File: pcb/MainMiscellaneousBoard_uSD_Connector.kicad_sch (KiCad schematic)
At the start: 10 parts, among them J1 0472192001

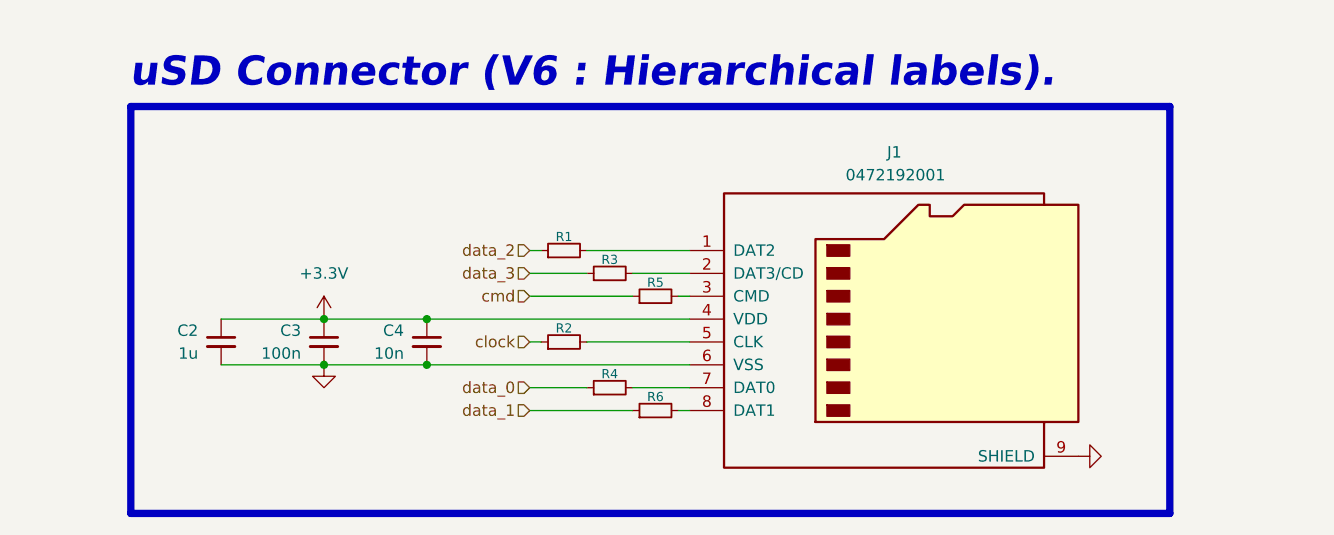
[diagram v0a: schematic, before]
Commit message: Updated `StackConnector` to use reference prefix of "J".
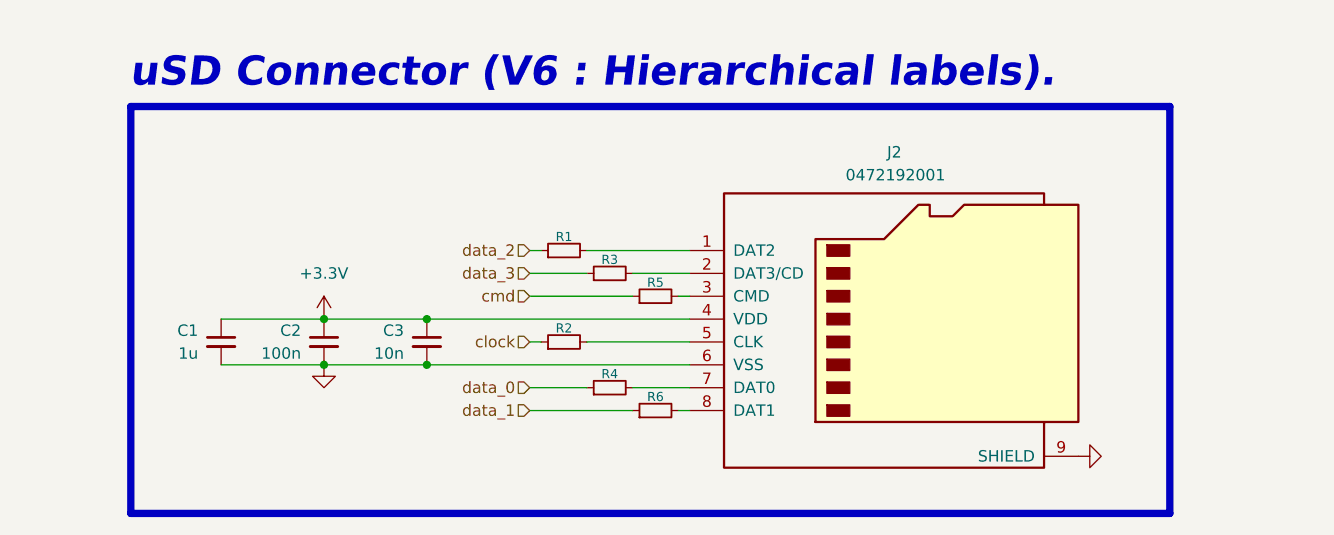
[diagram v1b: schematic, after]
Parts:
- renumbered C2 to C1, C3 to C2, C4 to C3, J1 to J2
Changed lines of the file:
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@@
 		(on_board yes)
 		(dnp no)
-		(property "Reference" "C2"
+		(property "Reference" "C1"
 			(at 52.07 78.7462 0)
 			(effects
@@
 			(project "MainMiscellaneousBoard"
 				(path "/98fc9565-7d66-4cd3-b0d6-fc60566bea9b/4f2e1eb9-ac73-426b-a6fe-8e3837c7983e"
-					(reference "C5")
-					(unit 1)
-				)
-				(path "/98fc9565-7d66-4cd3-b0d6-fc60566bea9b/5d94b41c-643f-433f-ba9e-5a80a87c9806"
-					(reference "C2")
+					(reference "C4")
+					(unit 1)
+				)
+				(path "/98fc9565-7d66-4cd3-b0d6-fc60566bea9b/5d94b41c-643f-433f-ba9e-5a80a87c9806"
+					(reference "C1")
 					(unit 1)
 				)
@@
 		(on_board yes)
 		(dnp no)
-		(property "Reference" "C3"
+		(property "Reference" "C2"
 			(at 63.5 78.7462 0)
 			(effects
@@
 			(project "MainMiscellaneousBoard"
 				(path "/98fc9565-7d66-4cd3-b0d6-fc60566bea9b/4f2e1eb9-ac73-426b-a6fe-8e3837c7983e"
-					(reference "C6")
-					(unit 1)
-				)
-				(path "/98fc9565-7d66-4cd3-b0d6-fc60566bea9b/5d94b41c-643f-433f-ba9e-5a80a87c9806"
-					(reference "C3")
+					(reference "C5")
+					(unit 1)
+				)
+				(path "/98fc9565-7d66-4cd3-b0d6-fc60566bea9b/5d94b41c-643f-433f-ba9e-5a80a87c9806"
+					(reference "C2")
 					(unit 1)
 				)
@@
 		(on_board yes)
 		(dnp no)
-		(property "Reference" "J1"
+		(property "Reference" "J2"
 			(at 129.413 58.928 0)
 			(effects
@@
 			(project "MainMiscellaneousBoard"
 				(path "/98fc9565-7d66-4cd3-b0d6-fc60566bea9b/4f2e1eb9-ac73-426b-a6fe-8e3837c7983e"
+					(reference "J3")
+					(unit 1)
+				)
+				(path "/98fc9565-7d66-4cd3-b0d6-fc60566bea9b/5d94b41c-643f-433f-ba9e-5a80a87c9806"
 					(reference "J2")
-					(unit 1)
-				)
-				(path "/98fc9565-7d66-4cd3-b0d6-fc60566bea9b/5d94b41c-643f-433f-ba9e-5a80a87c9806"
-					(reference "J1")
 					(unit 1)
 				)
@@
 		(on_board yes)
 		(dnp no)
-		(property "Reference" "C4"
+		(property "Reference" "C3"
 			(at 74.93 78.7462 0)
 			(effects
@@
 			(project "MainMiscellaneousBoard"
 				(path "/98fc9565-7d66-4cd3-b0d6-fc60566bea9b/4f2e1eb9-ac73-426b-a6fe-8e3837c7983e"
-					(reference "C7")
-					(unit 1)
-				)
-				(path "/98fc9565-7d66-4cd3-b0d6-fc60566bea9b/5d94b41c-643f-433f-ba9e-5a80a87c9806"
-					(reference "C4")
-					(unit 1)
-				)
+					(reference "C6")
+					(unit 1)
+				)
+				(path "/98fc9565-7d66-4cd3-b0d6-fc60566bea9b/5d94b41c-643f-433f-ba9e-5a80a87c9806"
+					(reference "C3")
+					(unit 1)
+				)

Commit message: Made symbol for ItsyBitsy ESP32.
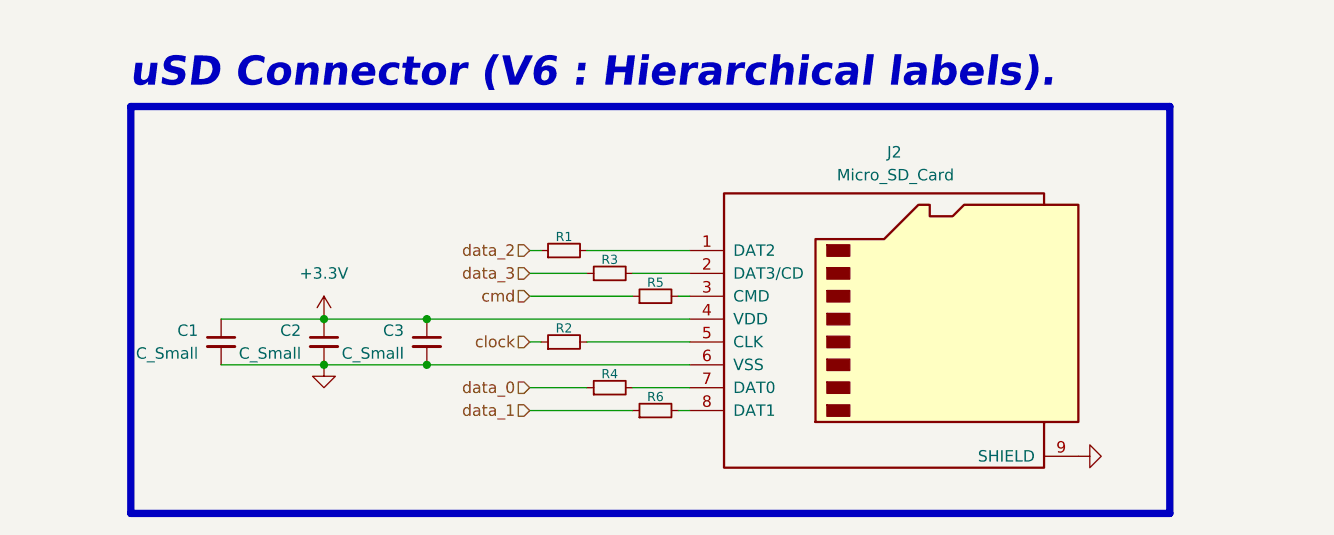
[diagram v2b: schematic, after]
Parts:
- C1: value 1u -> C_Small
- C2: value 100n -> C_Small
- C3: value 10n -> C_Small
- J2: value 0472192001 -> Micro_SD_Card
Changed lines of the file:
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@@
 			)
 		)
-		(property "Value" "1u"
+		(property "Value" "C_Small"
 			(at 52.07 81.2862 0)
 			(effects
@@
 			)
 		)
-		(property "Value" "100n"
+		(property "Value" "C_Small"
 			(at 63.5 81.2862 0)
 			(effects
@@
 			)
 		)
-		(property "Value" "0472192001"
+		(property "Value" "Micro_SD_Card"
 			(at 129.54 61.468 0)
 			(effects
@@
 		(dnp no)
 		(fields_autoplaced yes)
-		(property "Reference" "#PWR02"
+		(property "Reference" "#PWR2"
 			(at 66.04 88.9 0)
 			(effects
@@
 			(project "MainMiscellaneousBoard"
 				(path "/98fc9565-7d66-4cd3-b0d6-fc60566bea9b/4f2e1eb9-ac73-426b-a6fe-8e3837c7983e"
-					(reference "#PWR05")
-					(unit 1)
-				)
-				(path "/98fc9565-7d66-4cd3-b0d6-fc60566bea9b/5d94b41c-643f-433f-ba9e-5a80a87c9806"
-					(reference "#PWR02")
+					(reference "#PWR5")
+					(unit 1)
+				)
+				(path "/98fc9565-7d66-4cd3-b0d6-fc60566bea9b/5d94b41c-643f-433f-ba9e-5a80a87c9806"
+					(reference "#PWR2")
 					(unit 1)
 				)
@@
 		(dnp no)
 		(fields_autoplaced yes)
-		(property "Reference" "#PWR01"
+		(property "Reference" "#PWR1"
 			(at 66.04 81.28 0)
 			(effects
@@
 			(project "MainMiscellaneousBoard"
 				(path "/98fc9565-7d66-4cd3-b0d6-fc60566bea9b/4f2e1eb9-ac73-426b-a6fe-8e3837c7983e"
-					(reference "#PWR04")
-					(unit 1)
-				)
-				(path "/98fc9565-7d66-4cd3-b0d6-fc60566bea9b/5d94b41c-643f-433f-ba9e-5a80a87c9806"
-					(reference "#PWR01")
+					(reference "#PWR4")
+					(unit 1)
+				)
+				(path "/98fc9565-7d66-4cd3-b0d6-fc60566bea9b/5d94b41c-643f-433f-ba9e-5a80a87c9806"
+					(reference "#PWR1")
 					(unit 1)
 				)
@@
 		(dnp no)
 		(fields_autoplaced yes)
-		(property "Reference" "#PWR03"
+		(property "Reference" "#PWR3"
 			(at 156.21 92.71 0)
 			(effects
@@
 			(project "MainMiscellaneousBoard"
 				(path "/98fc9565-7d66-4cd3-b0d6-fc60566bea9b/4f2e1eb9-ac73-426b-a6fe-8e3837c7983e"
-					(reference "#PWR06")
-					(unit 1)
-				)
-				(path "/98fc9565-7d66-4cd3-b0d6-fc60566bea9b/5d94b41c-643f-433f-ba9e-5a80a87c9806"
-					(reference "#PWR03")
+					(reference "#PWR6")
+					(unit 1)
+				)
+				(path "/98fc9565-7d66-4cd3-b0d6-fc60566bea9b/5d94b41c-643f-433f-ba9e-5a80a87c9806"
+					(reference "#PWR3")
 					(unit 1)
 				)
@@
 			)
 		)
-		(property "Value" "10n"
+		(property "Value" "C_Small"
 			(at 74.93 81.2862 0)
 			(effects

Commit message: Fixed `MainMiscellaneousBoard_uSD_Connector.kicad_sch`; removed silkscreen for edge connector of `MainMiscellaneousBoard`.
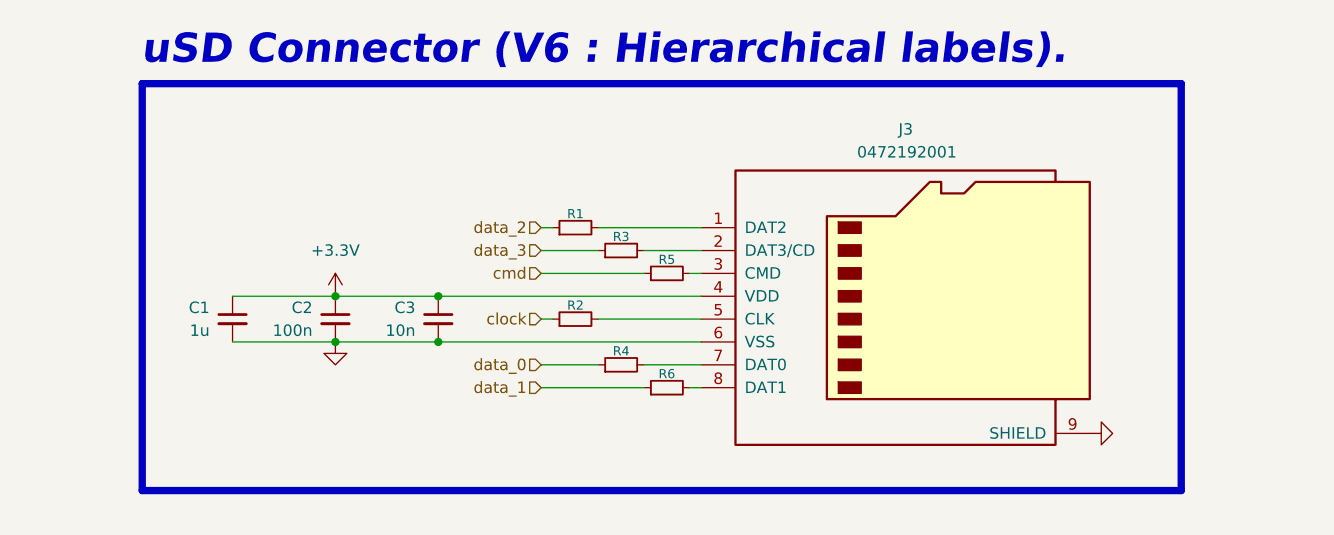
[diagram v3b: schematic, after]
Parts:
- C1: value C_Small -> 1u
- C2: value C_Small -> 100n
- C3: value C_Small -> 10n
- J3: renamed from J2; value Micro_SD_Card -> 0472192001
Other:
- moved on the sheet: C1, C2, C3, J3, R1, R2, R3, R4, R5, R6

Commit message: Adapted changes from `MainFlightComputer` into `MainMiscellaneousBoard`.
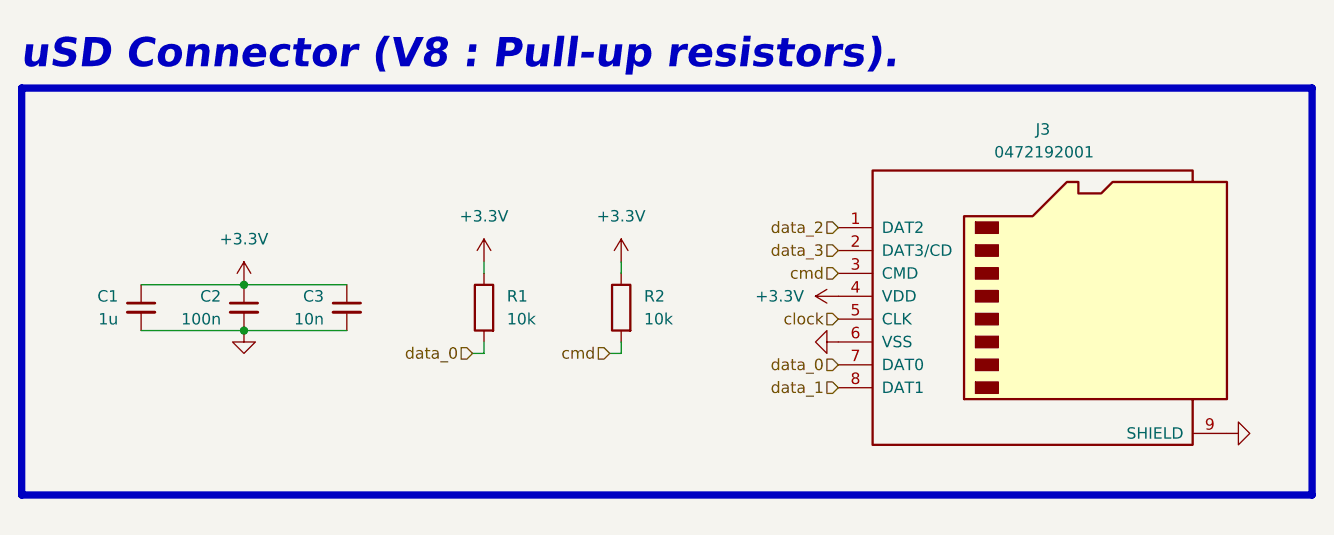
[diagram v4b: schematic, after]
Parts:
- removed R1, R2, R3, R4, R5, R6: R_Small, Resistor_SMD:R_1206_3216Metric_Pad1.30x1.75mm_HandSolder, symbol Device:R_Small
- added R1, R2: 10k, Resistor_SMD:R_1206_3216Metric_Pad1.30x1.75mm_HandSolder, symbol Device:R
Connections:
- net +3.3V: now also R1.1, R2.1
- net clock: now also J3.5 (CLK)
- net cmd: now also J3.3 (CMD), R2.2
- net data_0: now also J3.7 (DAT0), R1.2
- net data_1: now also J3.8 (DAT1)
- net data_2: now also J3.1 (DAT2)
- net data_3: now also J3.2 (DAT3/CD)
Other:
- note added: "uSD Connector (V8 : Pull-up resistors)."
- note removed: "uSD Connector (V6 : Hierarchical labels)."
- moved on the sheet: C1, C2, C3, J3

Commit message: Mostly finalized up `MainMiscellaneousBoard`.
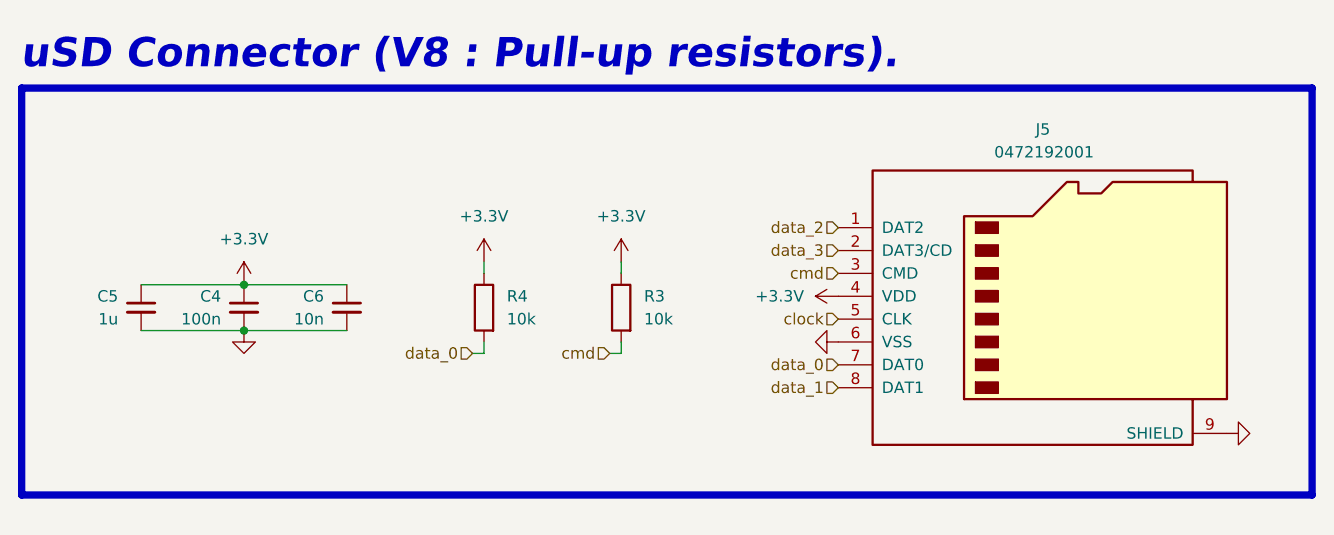
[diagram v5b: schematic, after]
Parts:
- renumbered C2 to C4, C1 to C5, C3 to C6, J3 to J5, R2 to R3, R1 to R4
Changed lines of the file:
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@@
 		(on_board yes)
 		(dnp no)
-		(property "Reference" "R2"
+		(property "Reference" "R3"
 			(at 101.6 74.9299 0)
 			(effects
@@
 			(project ""
 				(path "/98fc9565-7d66-4cd3-b0d6-fc60566bea9b/4f2e1eb9-ac73-426b-a6fe-8e3837c7983e"
-					(reference "R4")
-					(unit 1)
-				)
-				(path "/98fc9565-7d66-4cd3-b0d6-fc60566bea9b/5d94b41c-643f-433f-ba9e-5a80a87c9806"
 					(reference "R2")
+					(unit 1)
+				)
+				(path "/98fc9565-7d66-4cd3-b0d6-fc60566bea9b/5d94b41c-643f-433f-ba9e-5a80a87c9806"
+					(reference "R3")
 					(unit 1)
 				)
@@
 		(on_board yes)
 		(dnp no)
-		(property "Reference" "C1"
+		(property "Reference" "C5"
 			(at 43.18 74.9362 0)
 			(effects
@@
 			(project ""
 				(path "/98fc9565-7d66-4cd3-b0d6-fc60566bea9b/4f2e1eb9-ac73-426b-a6fe-8e3837c7983e"
-					(reference "C4")
-					(unit 1)
-				)
-				(path "/98fc9565-7d66-4cd3-b0d6-fc60566bea9b/5d94b41c-643f-433f-ba9e-5a80a87c9806"
 					(reference "C1")
+					(unit 1)
+				)
+				(path "/98fc9565-7d66-4cd3-b0d6-fc60566bea9b/5d94b41c-643f-433f-ba9e-5a80a87c9806"
+					(reference "C5")
 					(unit 1)
 				)
@@
 		(on_board yes)
 		(dnp no)
-		(property "Reference" "C2"
+		(property "Reference" "C4"
 			(at 54.61 74.9362 0)
 			(effects
@@
 			(project ""
 				(path "/98fc9565-7d66-4cd3-b0d6-fc60566bea9b/4f2e1eb9-ac73-426b-a6fe-8e3837c7983e"
-					(reference "C5")
-					(unit 1)
-				)
-				(path "/98fc9565-7d66-4cd3-b0d6-fc60566bea9b/5d94b41c-643f-433f-ba9e-5a80a87c9806"
 					(reference "C2")
+					(unit 1)
+				)
+				(path "/98fc9565-7d66-4cd3-b0d6-fc60566bea9b/5d94b41c-643f-433f-ba9e-5a80a87c9806"
+					(reference "C4")
 					(unit 1)
 				)
@@
 		(on_board yes)
 		(dnp no)
-		(property "Reference" "J3"
+		(property "Reference" "J5"
 			(at 145.923 56.388 0)
 			(effects
@@
 			(project ""
 				(path "/98fc9565-7d66-4cd3-b0d6-fc60566bea9b/4f2e1eb9-ac73-426b-a6fe-8e3837c7983e"
-					(reference "J4")
-					(unit 1)
-				)
-				(path "/98fc9565-7d66-4cd3-b0d6-fc60566bea9b/5d94b41c-643f-433f-ba9e-5a80a87c9806"
-					(reference "J3")
+					(reference "J6")
+					(unit 1)
+				)
+				(path "/98fc9565-7d66-4cd3-b0d6-fc60566bea9b/5d94b41c-643f-433f-ba9e-5a80a87c9806"
+					(reference "J5")
 					(unit 1)
 				)
@@
 		(on_board yes)
 		(dnp no)
-		(property "Reference" "R1"
+		(property "Reference" "R4"
 			(at 86.36 74.9299 0)
 			(effects
@@
 			(project ""
 				(path "/98fc9565-7d66-4cd3-b0d6-fc60566bea9b/4f2e1eb9-ac73-426b-a6fe-8e3837c7983e"
-					(reference "R3")
-					(unit 1)
-				)
-				(path "/98fc9565-7d66-4cd3-b0d6-fc60566bea9b/5d94b41c-643f-433f-ba9e-5a80a87c9806"
 					(reference "R1")
+					(unit 1)
+				)
+				(path "/98fc9565-7d66-4cd3-b0d6-fc60566bea9b/5d94b41c-643f-433f-ba9e-5a80a87c9806"
+					(reference "R4")
 					(unit 1)
 				)
@@
 		(on_board yes)
 		(dnp no)
-		(property "Reference" "C3"
+		(property "Reference" "C6"
 			(at 66.04 74.9362 0)
 			(effects
@@
 			(project ""
 				(path "/98fc9565-7d66-4cd3-b0d6-fc60566bea9b/4f2e1eb9-ac73-426b-a6fe-8e3837c7983e"
+					(reference "C3")
+					(unit 1)
+				)
+				(path "/98fc9565-7d66-4cd3-b0d6-fc60566bea9b/5d94b41c-643f-433f-ba9e-5a80a87c9806"
 					(reference "C6")
 					(unit 1)
 				)
-				(path "/98fc9565-7d66-4cd3-b0d6-fc60566bea9b/5d94b41c-643f-433f-ba9e-5a80a87c9806"
-					(reference "C3")
-					(unit 1)
-				)
